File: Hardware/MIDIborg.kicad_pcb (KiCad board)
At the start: 4 copper layers, 50.8 x 50.8 mm, 50 parts, among them J2 8P8C, J4 8P8C, J5 Conn_ARM_JTAG_SWD_10, J6 Conn_01x11, J7 8P8C, J8 Conn_01x03, J9 Conn_01x11, P1 USB_C_Plug_USB2.0, Q1 2N7002, SW1 SW_Push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

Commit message: Finished layout
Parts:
- removed TP1: TestPoint, TestPoint:TestPoint_Pad_D1.5mm
- added C14: .1uF, Capacitor_SMD:C_0402_1005Metric_Pad0.74x0.62mm_HandSolder, F.Cu at (231.1, 89.9)
- C11, C12, C4, TP3: moved to B.Cu
- moved R3 147.2 mm to (229.8, 88.0), turned to 180 degrees
- moved R11 142.5 mm to (230.1, 101.8), turned to 180 degrees
- moved R4 141.3 mm to (225.7, 86.5), turned to -90 degrees
- moved R9 128.1 mm to (215.3, 95.4), turned to 90 degrees
- moved R10 126.8 mm to (213.5, 94.8)
- moved R8 125.5 mm to (211.4, 99.9), turned to -90 degrees
- moved TP4 124.6 mm to (239.6, 93.2)
- moved TP7 124.5 mm to (239.6, 90.2)
- moved TP3 119.9 mm to (234.8, 78.3), turned to 180 degrees
- moved TP5 109.4 mm to (236.6, 93.1)
- moved C12 107.2 mm to (227.2, 101.8), turned to 90 degrees
- moved C7 106.8 mm to (233.1, 92.7), turned to 180 degrees
- moved C4 102.0 mm to (226.2, 101.8), turned to 90 degrees
- moved R5 100.3 mm to (229.8, 86.6)
- moved C6 97.0 mm to (229.9, 89.9), turned to -90 degrees
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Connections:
- C10 pad 1: Net-(C10-Pad1) -> GND
- C12 pad 1: Net-(C10-Pad1) -> GND
- C13 pad 1: Net-(C10-Pad1) -> GND
- C4 pad 1: Net-(C10-Pad1) -> GND
- C5 pad 1: Net-(C10-Pad1) -> GND
- C6 pad 1: Net-(C10-Pad1) -> GND
- C7 pad 1: Net-(C10-Pad1) -> GND
- C8 pad 1: Net-(C10-Pad1) -> GND
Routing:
- net /ADC3: track 0.00 -> 47.4 mm, vias 0 -> 4
- net /ADC1: track 0.00 -> 45.2 mm, vias 0 -> 3
- net /SWCLK: track 0.00 -> 42.5 mm, vias 0 -> 2
- net /ADC2: track 0.00 -> 42.2 mm, vias 0 -> 3
- net +3V3: track 7.77 -> 49.4 mm, vias 1 -> 23
- net /SPI0_NSS: track 0.00 -> 35.1 mm, vias 0 -> 4
- net /ADC0: track 0.00 -> 34.3 mm, vias 0 -> 3
- net /SPI0_MISO: track 0.00 -> 32.3 mm, vias 0 -> 1
- net /SPI0_MOSI: track 0.00 -> 31.7 mm, vias 0 -> 3
- net /SPI0_SCK: track 0.00 -> 31.3 mm, vias 0 -> 1
- net /GPIO24: track 0.00 -> 30.3 mm
- net /SWDIO: track 0.00 -> 30.2 mm, vias 0 -> 2
- net /GPIO22: track 0.00 -> 29.3 mm, vias 0 -> 2
- net /GPIO25: track 0.00 -> 28.8 mm
- net /UART1_TX: track 0.00 -> 28.0 mm, vias 0 -> 1
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- added copper zone on In2.Cu, net +3V3

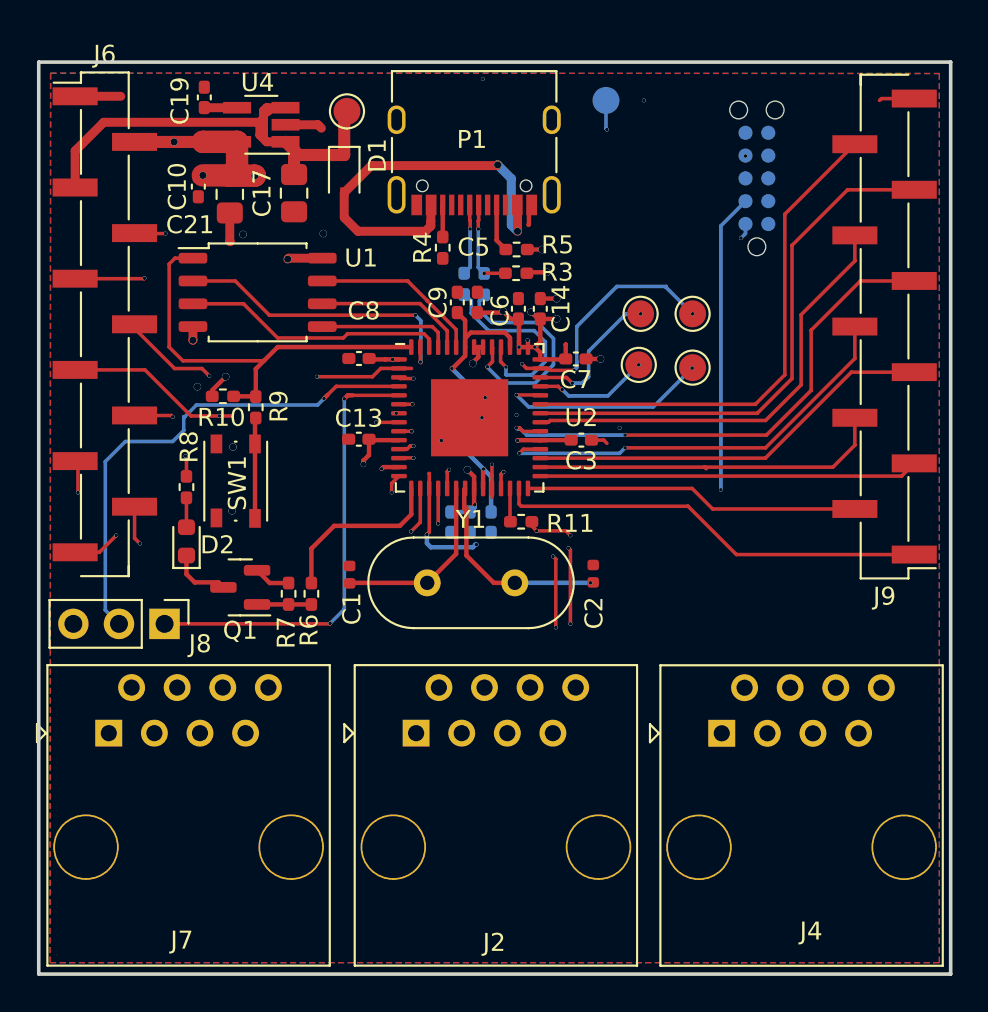
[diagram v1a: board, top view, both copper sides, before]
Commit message: One layer Midiborg
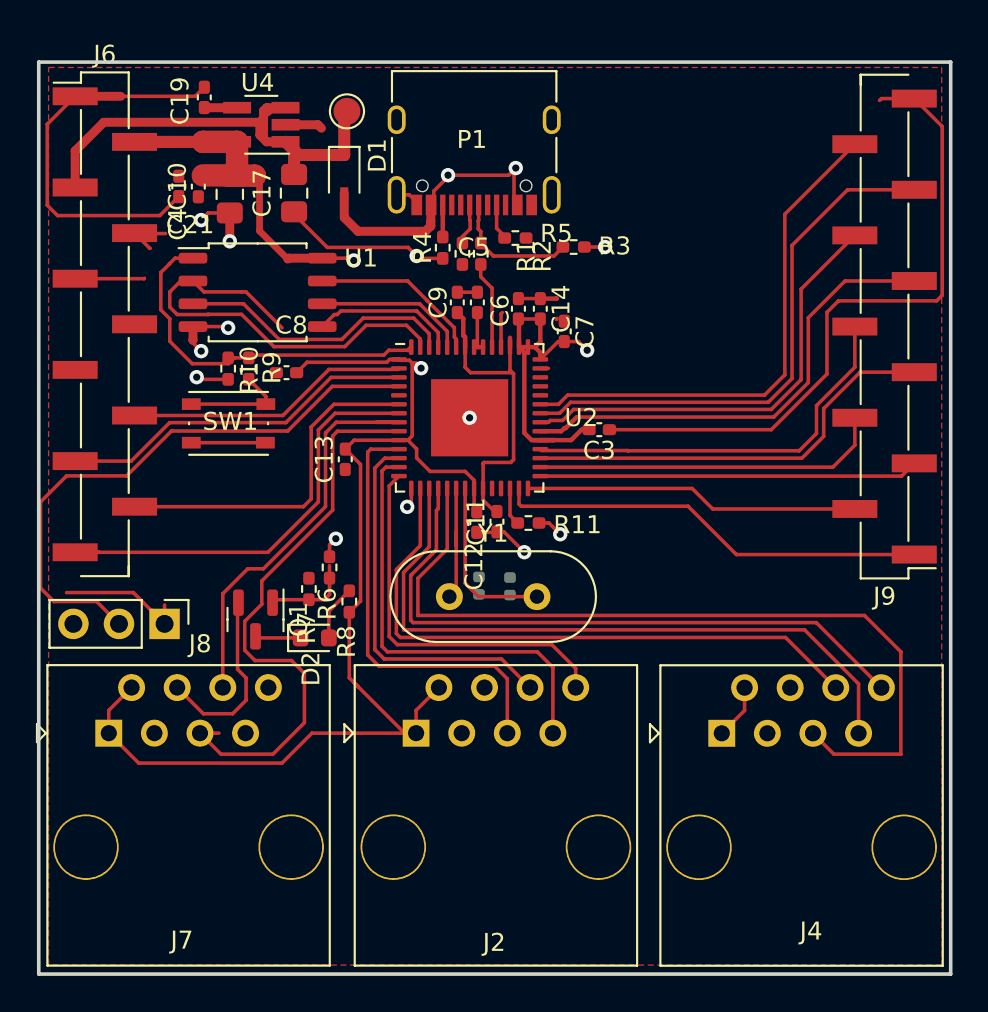
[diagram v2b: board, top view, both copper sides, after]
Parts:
- removed J5: Conn_ARM_JTAG_SWD_10, Connector:Tag-Connect_TC2050-IDC-NL_2x05_P1.27mm_Vertical
- removed TP3, TP4, TP5, TP6, TP7: TestPoint, TestPoint:TestPoint_Pad_D1.5mm
- C1, C2: moved to B.Cu
- C11, C12, C4, R1, R2: moved to F.Cu
- moved C4 24.1 mm to (211.0, 83.1)
- moved R8 11.1 mm to (220.5, 106.2), turned to 90 degrees
- moved D2 8.94 mm to (218.6, 108.3), turned to 0 degrees
- moved C1 7.23 mm to (227.7, 105.4)
- moved C2 4.69 mm to (229.4, 105.4)
- moved C8 4.12 mm to (217.0, 93.5)
- moved R3 3.52 mm to (233.0, 86.5)
- moved SW1 3.24 mm to (213.8, 96.3), turned to 0 degrees
- moved R9 2.19 mm to (214.9, 93.3)
- moved Q1 1.98 mm to (215.3, 107.2), turned to -90 degrees
- moved R6 1.78 mm to (219.4, 104.3)
- moved R2 1.71 mm to (227.8, 86.9)
- moved R1 1.68 mm to (226.8, 86.9)
- moved C7 1.67 mm to (232.5, 91.2), turned to -90 degrees
- moved R10 1.57 mm to (213.8, 93.3), turned to 90 degrees
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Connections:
- J6 pad 10: /ADC2 -> /GPIO4
- J6 pad 11: /ADC3 -> /GPIO5
- J6 pad 4: /GPIO0 -> unconnected-(J6-Pad4)
- J6 pad 5: /GPIO1 -> unconnected-(J6-Pad5)
- J6 pad 6: /GPIO4 -> unconnected-(J6-Pad6)
- J6 pad 7: /GPIO5 -> unconnected-(J6-Pad7)
- J6 pad 8: /ADC0 -> /GPIO0
- J6 pad 9: /ADC1 -> /GPIO1
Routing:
- net GND: track 16.7 -> 103.8 mm, vias 16 -> 7
- net +3V3: track 49.4 -> 115.0 mm, vias 23 -> 6
- net /ADC3: track 47.4 -> 0.45 mm, vias 4 -> 0
- net /ADC1: track 45.2 -> 0.00 mm, vias 3 -> 0
- net /SWCLK: track 42.5 -> 0.00 mm, vias 2 -> 0
- net /ADC2: track 42.2 -> 0.01 mm, vias 3 -> 0
- net /ADC0: track 34.3 -> 0.03 mm, vias 3 -> 0
- net /SWDIO: track 30.2 -> 0.00 mm, vias 2 -> 0
- net /UART1_RX: track 25.2 -> 7.23 mm, vias 2 -> 0
- net /SPI0_MOSI: track 31.7 -> 46.6 mm, vias 3 -> 0
- net /d-: track 11.2 -> 1.99 mm, vias 1 -> 0
- net /d+: track 13.0 -> 4.90 mm, vias 1 -> 0
- net /QSPI-SD1: track 16.8 -> 24.6 mm, vias 2 -> 0
- net /LED1: track 9.84 -> 2.26 mm, vias 0 -> 2
- net /GPIO0: track 21.5 -> 15.8 mm, vias 2 -> 0
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- removed copper zone on In1.Cu, net +3V3
- removed copper zone on In2.Cu, net +3V3
- removed copper zone on B.Cu, net GND
